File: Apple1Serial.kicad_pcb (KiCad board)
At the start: 2 copper layers, 148.8 x 77.7 mm, 35 parts, among them U7402 7402

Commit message: Fixed element values on schematics
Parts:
- 74S257mux1, 74S257mux2, 8T97buf1, 8T97buf2: footprint Package_DIP:DIP-16_W7.62mm_Socket_LongPads -> Package_DIP:DIP-16_W7.62mm_LongPads
- AT28C64B1: footprint Package_DIP:DIP-28_W15.24mm_Socket_LongPads -> Package_DIP:DIP-28_W15.24mm_LongPads
- ATmega328P1: footprint Package_DIP:DIP-28_W7.62mm_Socket_LongPads -> Package_DIP:DIP-28_W7.62mm_LongPads
- GAL20V8B1: footprint Package_DIP:DIP-24_W7.62mm_Socket_LongPads -> Package_DIP:DIP-24_W7.62mm_LongPads
- LED1: footprint Package_DIP:DIP-8_W7.62mm_Socket_LongPads -> Package_DIP:DIP-8_W7.62mm_LongPads
- U7402: footprint Package_DIP:DIP-14_W7.62mm_Socket_LongPads -> Package_DIP:DIP-14_W7.62mm_LongPads

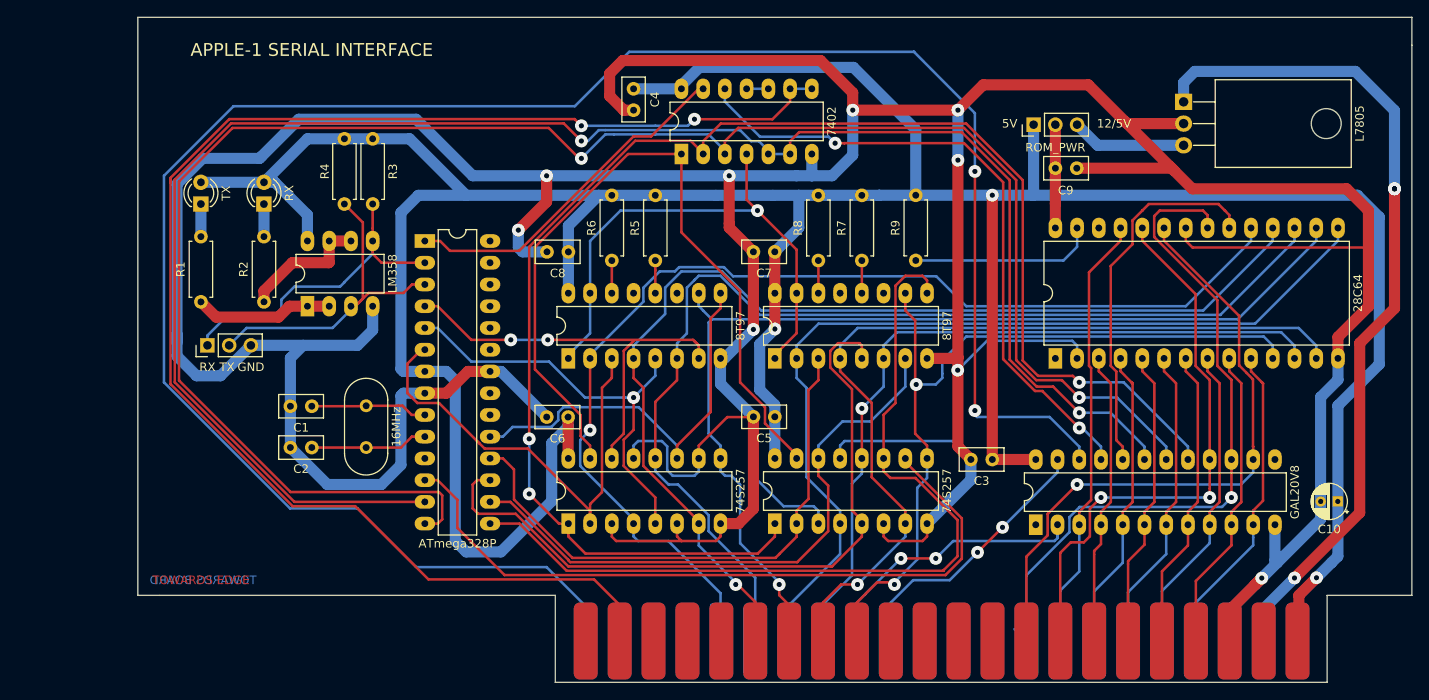
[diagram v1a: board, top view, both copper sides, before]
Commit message: Added DB9 rs232 connector
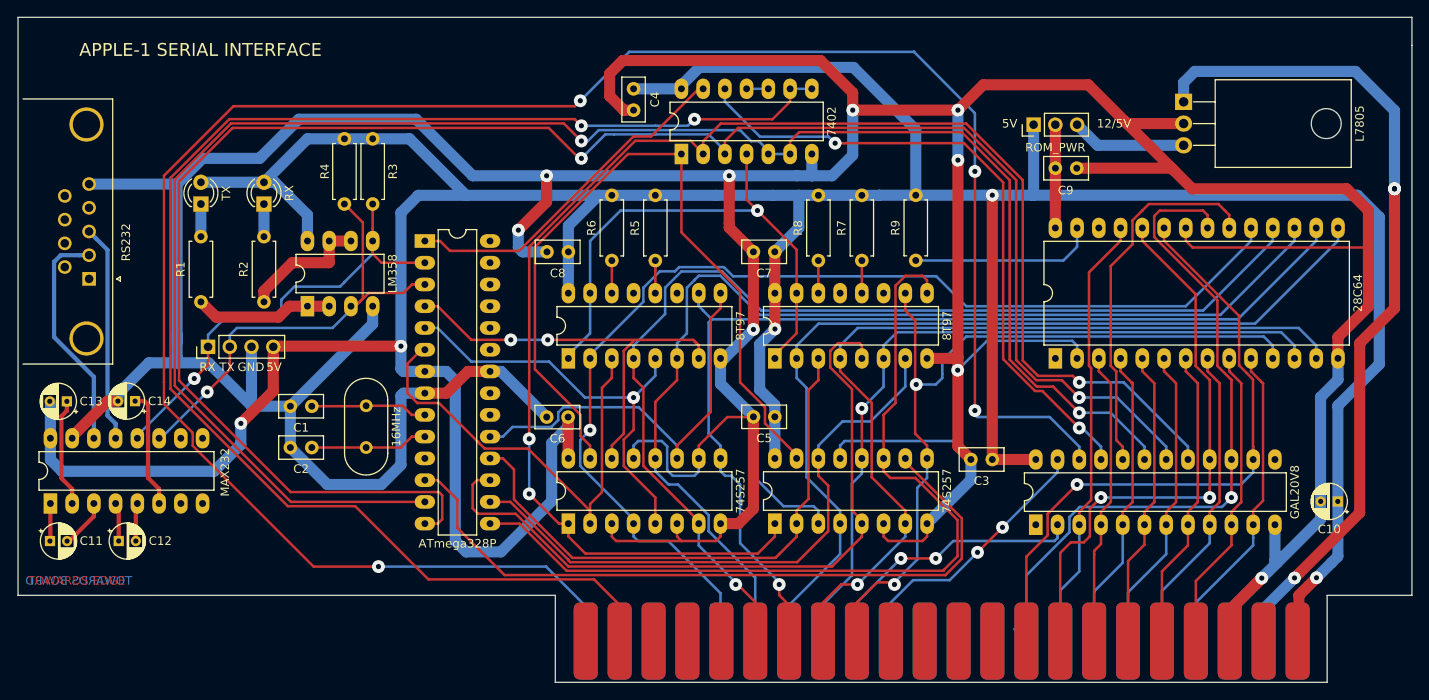
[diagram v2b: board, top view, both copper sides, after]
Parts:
- added C11: 10uF, Capacitor_THT:CP_Radial_D4.0mm_P2.00mm, F.Cu at (54.2, 106.4)
- added C12: 10uF, Capacitor_THT:CP_Radial_D4.0mm_P2.00mm, F.Cu at (62.3, 106.4)
- added C13: 10uF, Capacitor_THT:CP_Radial_D4.0mm_P2.00mm, F.Cu at (56.2, 90.1)
- added C14: 10uF, Capacitor_THT:CP_Radial_D4.0mm_P2.00mm, F.Cu at (64.2, 90.1)
- added MAX232: MAX232, Package_DIP:DIP-16_W7.62mm_LongPads, F.Cu at (54.3, 102.0)
- added RS232: DB9_Female_MountingHoles, Connector_Dsub:DSUB-9_Female_Horizontal_P2.77x2.84mm_EdgePinOffset4.94mm_Housed_MountingHolesOffset7.48mm, F.Cu at (58.8, 75.8)
- SERIAL1: value SERIAL -> SERIAL1; footprint Connector_PinHeader_2.54mm:PinHeader_1x03_P2.54mm_Vertical -> Connector_PinHeader_2.54mm:PinHeader_1x04_P2.54mm_Vertical
- moved SERIAL1 0.18 mm to (72.7, 83.7)
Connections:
- net R renamed T
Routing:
- net +5V: track 424.3 -> 483.2 mm, vias 3 -> 5
- net GND: track 645.6 -> 674.7 mm
- net Net-(RS232-Pad2): track 0.00 -> 26.9 mm
- net Net-(RS232-Pad3): track 0.00 -> 25.4 mm
- net /TXD: track 38.9 -> 53.9 mm, vias 0 -> 1
- net /RXD: track 38.9 -> 53.5 mm, vias 0 -> 1
- net Net-(C14-Pad1): track 0.00 -> 13.8 mm
- net Net-(C13-Pad1): track 0.00 -> 12.7 mm
- net Net-(C11-Pad2): track 0.00 -> 5.83 mm
- net Net-(C12-Pad1): track 0.00 -> 4.53 mm
- net Net-(C12-Pad2): track 0.00 -> 4.46 mm
- net Net-(C11-Pad1): track 0.00 -> 4.41 mm
- net PHI2: track 243.1 -> 245.5 mm, vias 2 -> 4
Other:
- board size 148.8 x 77.7 mm -> 162.8 x 77.7 mm
